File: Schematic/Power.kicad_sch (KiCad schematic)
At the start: 41 parts, among them IC1 MP9943AGQ-Z, IC2 MP9943AGQ-Z, U2 ME6217C33M5G, U3 LDO-1.8v

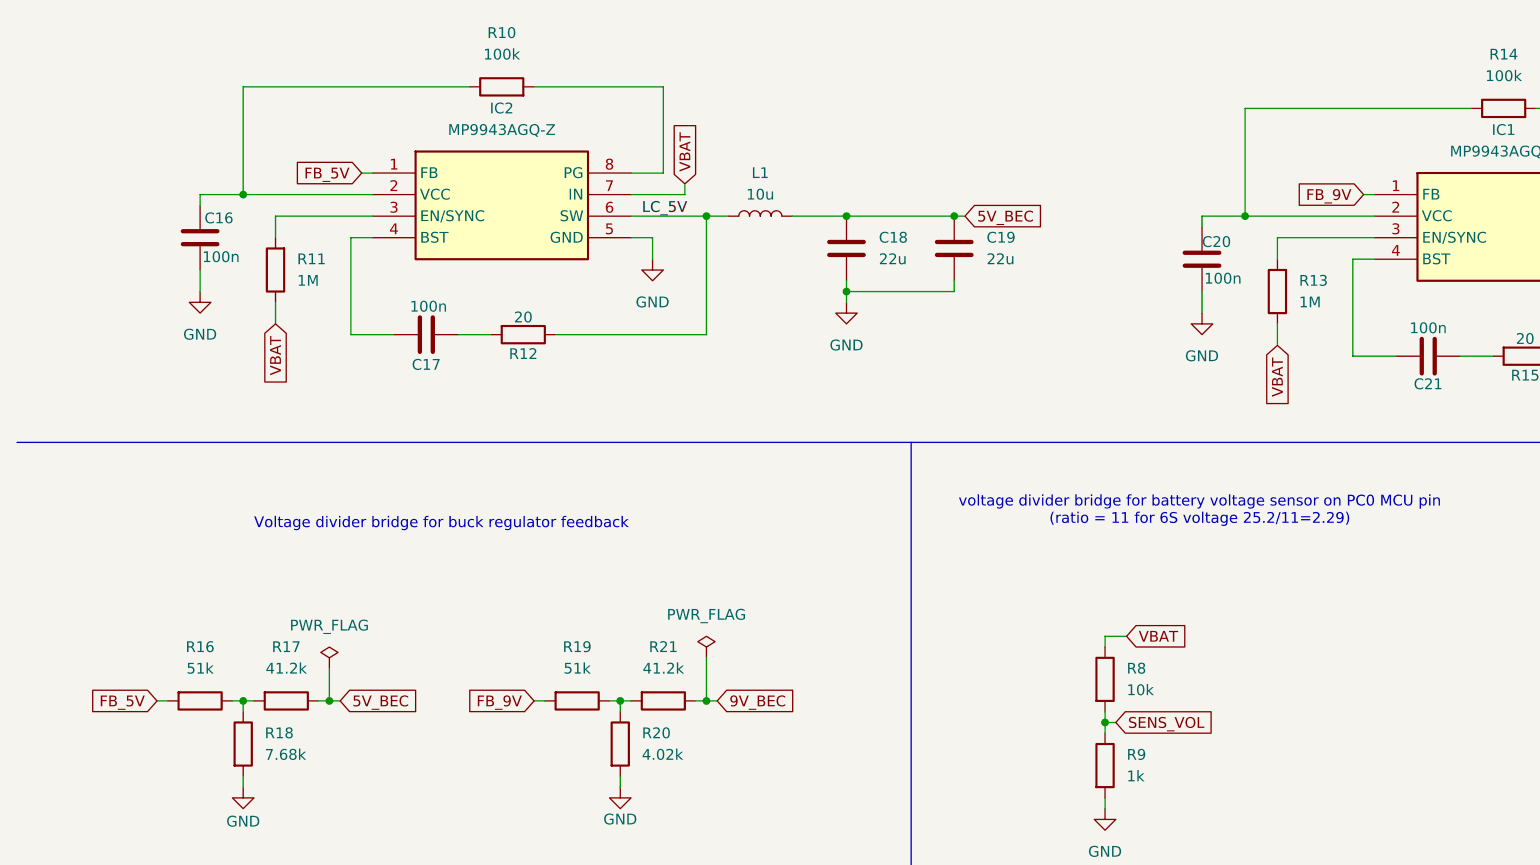
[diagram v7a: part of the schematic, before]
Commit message: pcb layout refactoring
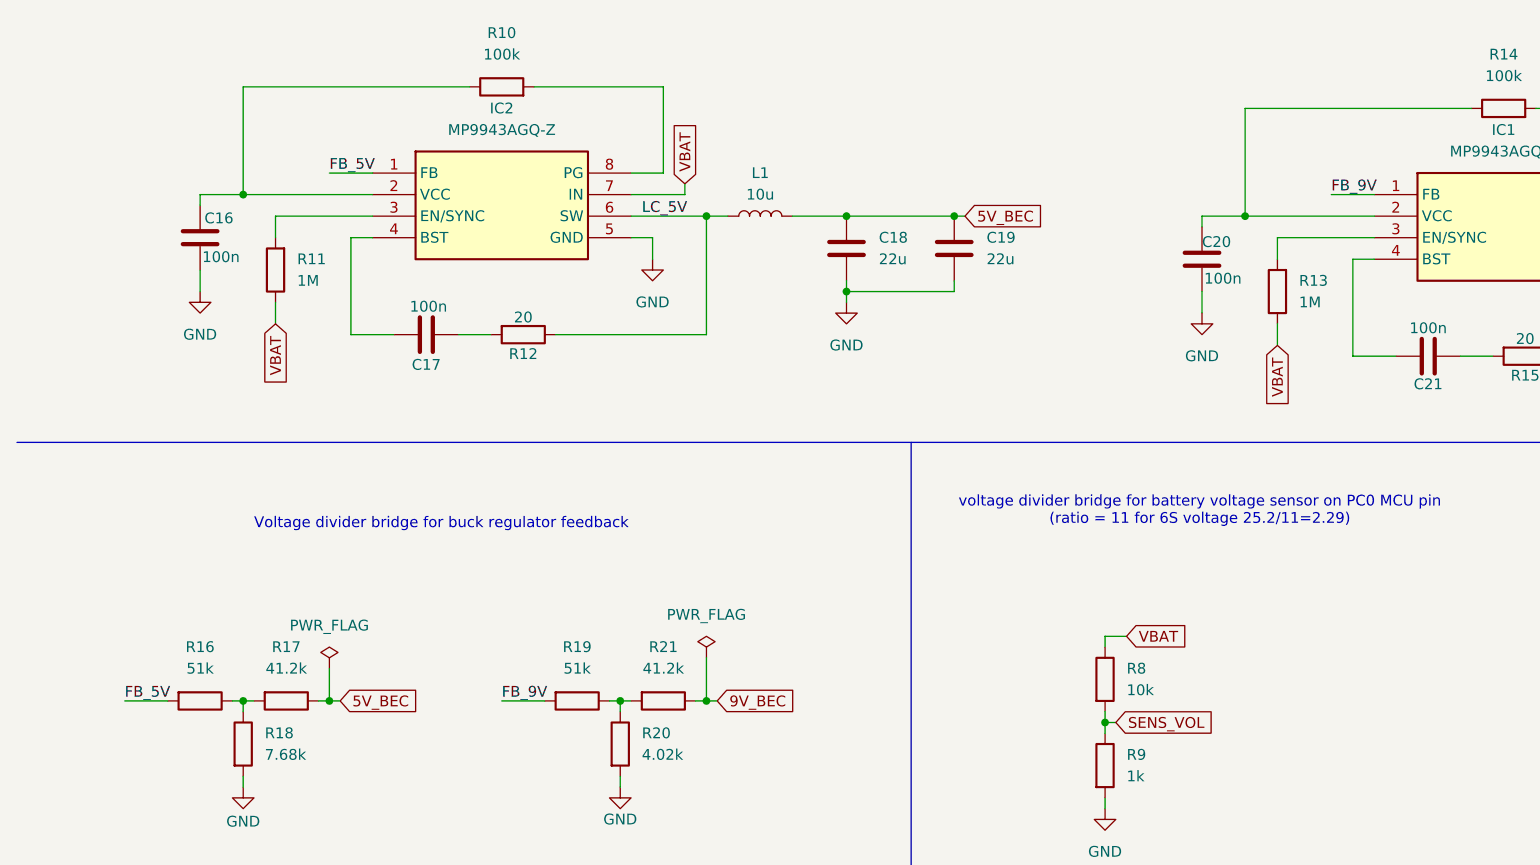
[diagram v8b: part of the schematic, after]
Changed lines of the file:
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@@
+	(wire
+		(pts
+			(xy 69.85 162.56) (xy 74.93 162.56)
+		)
+		(stroke
+			(width 0)
+			(type default)
+		)
+	)
 	(wire
 		(pts
@@
 	(wire
 		(pts
+			(xy 167.64 102.87) (xy 172.72 102.87)
+		)
+		(stroke
+			(width 0)
+			(type default)
+		)
+	)
+	(wire
+		(pts
 			(xy 139.7 38.1) (xy 139.7 39.37)
 		)
@@
 	(wire
 		(pts
-			(xy 53.34 100.33) (xy 54.61 100.33)
-		)
-		(stroke
-			(width 0)
-			(type default)
-		)
-	)
-	(wire
-		(pts
-			(xy 73.66 162.56) (xy 74.93 162.56)
-		)
-		(stroke
-			(width 0)
-			(type default)
-		)
-	)
-	(wire
-		(pts
 			(xy 152.4 114.3) (xy 152.4 116.84)
 		)
@@
 	(wire
 		(pts
-			(xy 29.21 162.56) (xy 30.48 162.56)
-		)
-		(stroke
-			(width 0)
-			(type default)
-		)
-	)
-	(wire
-		(pts
 			(xy 140.97 154.94) (xy 143.51 154.94)
 		)
@@
 	(wire
 		(pts
+			(xy 25.4 162.56) (xy 30.48 162.56)
+		)
+		(stroke
+			(width 0)
+			(type default)
+		)
+	)
+	(wire
+		(pts
 			(xy 224.79 115.57) (xy 224.79 116.84)
 		)
@@
 	(wire
 		(pts
-			(xy 171.45 102.87) (xy 172.72 102.87)
-		)
-		(stroke
-			(width 0)
-			(type default)
-		)
-	)
-	(wire
-		(pts
 			(xy 203.2 105.41) (xy 209.55 105.41)
 		)
@@
 	(wire
 		(pts
+			(xy 49.53 100.33) (xy 54.61 100.33)
+		)
+		(stroke
+			(width 0)
+			(type default)
+		)
+	)
+	(wire
+		(pts
 			(xy 157.48 105.41) (xy 172.72 105.41)
 		)
@@
 			(width 0)
 			(type default)
+		)
+	)
+	(label "FB_9V"
+		(at 167.64 102.87 0)
+		(effects
+			(font
+				(size 1.27 1.27)
+			)
+			(justify left bottom)
 		)
 	)
@@
 		)
 	)
-	(global_label "FB_5V"
-		(shape input)
-		(at 29.21 162.56 180)
-		(fields_autoplaced yes)
-		(effects
-			(font
-				(size 1.27 1.27)
-			)
-			(justify right)
-		)
-		(property "Intersheetrefs" "${INTERSHEET_REFS}"
-			(at 20.6005 162.56 0)
-			(effects
-				(font
-					(size 1.27 1.27)
-				)
-				(justify right)
-				(hide yes)
-			)
+	(label "FB_5V"
+		(at 25.4 162.56 0)
+		(effects
+			(font
+				(size 1.27 1.27)
+			)
+			(justify left bottom)
+		)
+	)
+	(label "FB_9V"
+		(at 69.85 162.56 0)
+		(effects
+			(font
+				(size 1.27 1.27)
+			)
+			(justify left bottom)
+		)
+	)
+	(label "FB_5V"
+		(at 49.53 100.33 0)
+		(effects
+			(font
+				(size 1.27 1.27)
+			)
+			(justify left bottom)
 		)
 	)
@@
 		)
 	)
-	(global_label "FB_9V"
-		(shape input)
-		(at 171.45 102.87 180)
-		(fields_autoplaced yes)
-		(effects
-			(font
-				(size 1.27 1.27)
-			)
-			(justify right)
-		)
-		(property "Intersheetrefs" "${INTERSHEET_REFS}"
-			(at 162.8405 102.87 0)
-			(effects
-				(font
-					(size 1.27 1.27)
-				)
-				(justify right)
-				(hide yes)
-			)
-		)
-	)
 	(global_label "9V_BEC"
 		(shape input)
@@
 		)
 	)
-	(global_label "FB_9V"
-		(shape input)
-		(at 73.66 162.56 180)
-		(fields_autoplaced yes)
-		(effects
-			(font
-				(size 1.27 1.27)
-			)
-			(justify right)
-		)
-		(property "Intersheetrefs" "${INTERSHEET_REFS}"
-			(at 65.0505 162.56 0)
-			(effects
-				(font
-					(size 1.27 1.27)
-				)
-				(justify right)
-				(hide yes)
-			)
-		)
-	)
 	(global_label "VBAT"
 		(shape input)
@@
 				(hide yes)
 			)
-		)
-	)
-	(global_label "FB_5V"
-		(shape input)
-		(at 53.34 100.33 180)
-		(fields_autoplaced yes)
-		(effects
-			(font
-				(size 1.27 1.27)
-			)
-			(justify right)
-		)
-		(property "Intersheetrefs" "${INTERSHEET_REFS}"
-			(at 44.7305 100.33 0)
-			(effects
-				(font
-					(size 1.27 1.27)
-				)
-				(justify right)
-				(hide yes)
-			)
